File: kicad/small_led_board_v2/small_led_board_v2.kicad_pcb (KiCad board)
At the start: 2 copper layers, 83 parts, among them Q1 SQ2351CES, Q2 SQ2351CES, Q3 SQ2351CES, Q4 SQ2351CES, Q5 SQ2351CES, Q6 SQ2351CES, U1 74HCT541, U2 74HCT595, U3 TPIC6B595N

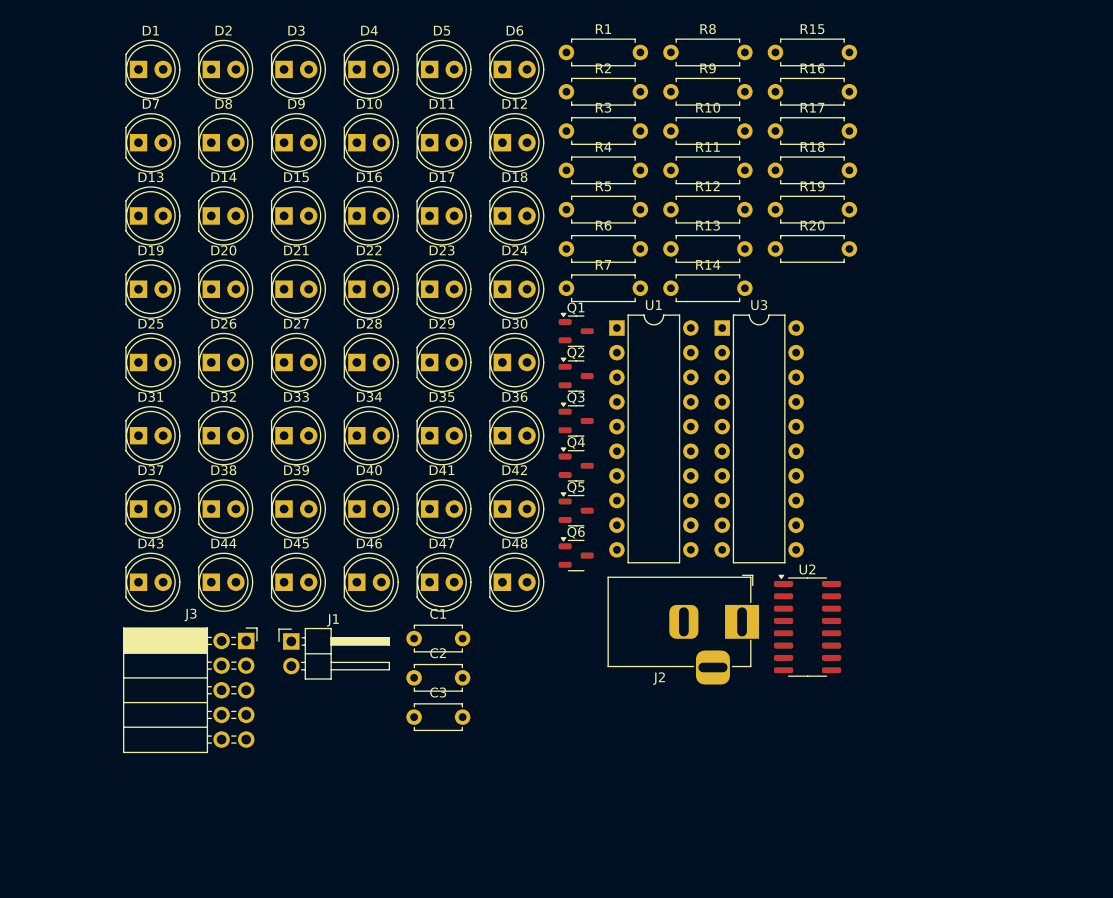
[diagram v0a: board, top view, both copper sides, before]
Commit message: small led board v2: placed components in general area
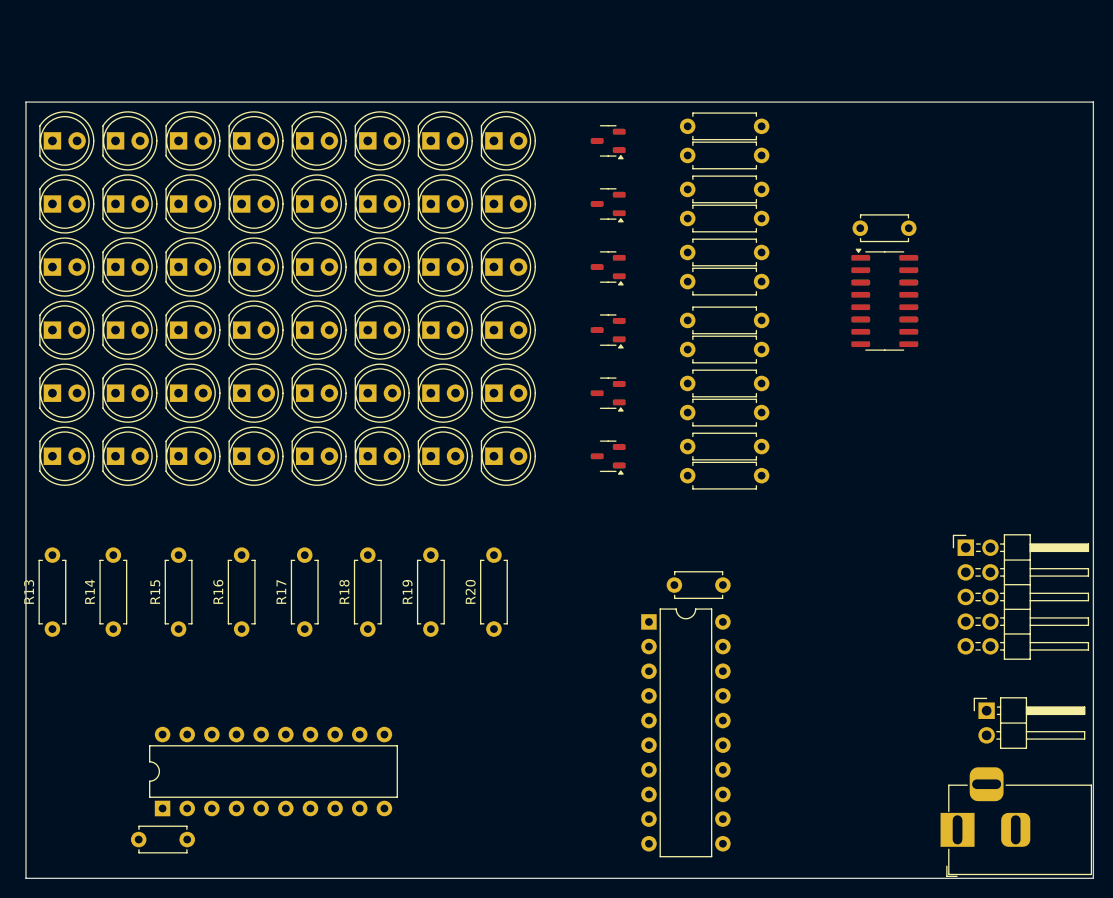
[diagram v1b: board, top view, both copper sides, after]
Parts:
- J3: footprint Connector_PinSocket_2.54mm:PinSocket_2x05_P2.54mm_Horizontal -> Connector_PinHeader_2.54mm:PinHeader_2x05_P2.54mm_Horizontal
- moved R15 85.5 mm to (65.7, 104.3), turned to 90 degrees
- moved R16 78.1 mm to (72.2, 104.3), turned to 90 degrees
- moved U3 76.0 mm to (64.1, 122.8), turned to 90 degrees
- moved R13 74.8 mm to (52.7, 104.3), turned to 90 degrees
- moved J3 74.8 mm to (146.8, 95.9)
- moved J1 72.0 mm to (149.0, 112.7)
- moved R17 70.6 mm to (78.7, 104.3), turned to 90 degrees
- moved C2 68.9 mm to (141.0, 63.0), turned to 180 degrees
- moved R14 67.3 mm to (59.0, 104.3), turned to 90 degrees
- moved R18 63.2 mm to (85.2, 104.3), turned to 90 degrees
- moved R19 55.9 mm to (91.7, 104.3), turned to 90 degrees
- moved R20 48.7 mm to (98.2, 104.3), turned to 90 degrees
- moved D42 40.2 mm to (59.2, 86.5)
- moved D18 40.2 mm to (59.2, 67.0)
- moved D41 39.2 mm to (52.7, 86.5)
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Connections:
- J3 pad 2: ShiftRowData -> RowStrobe
- J3 pad 3: ApplyRowAndStrobe -> ShiftRowData
- J3 pad 4: unconnected-(J3-Pin_4-Pad4) -> ShiftRowStrobe
- J3 pad 5: GND -> ApplyRowAndStrobe
- J3 pad 6: RowStrobe -> OutputEnable
- J3 pad 7: ShiftRowStrobe -> unconnected-(J3-Pin_7-Pad7)
- J3 pad 8: OutputEnable -> unconnected-(J3-Pin_8-Pad8)
- J3 pad 9: unconnected-(J3-Pin_9-Pad9) -> GND
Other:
- board outline added: 110 x 80 mm

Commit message: small led board v2: routing done and plotted
Also it was sent off to a manufacturer without major fixes. Just to see how it goes.
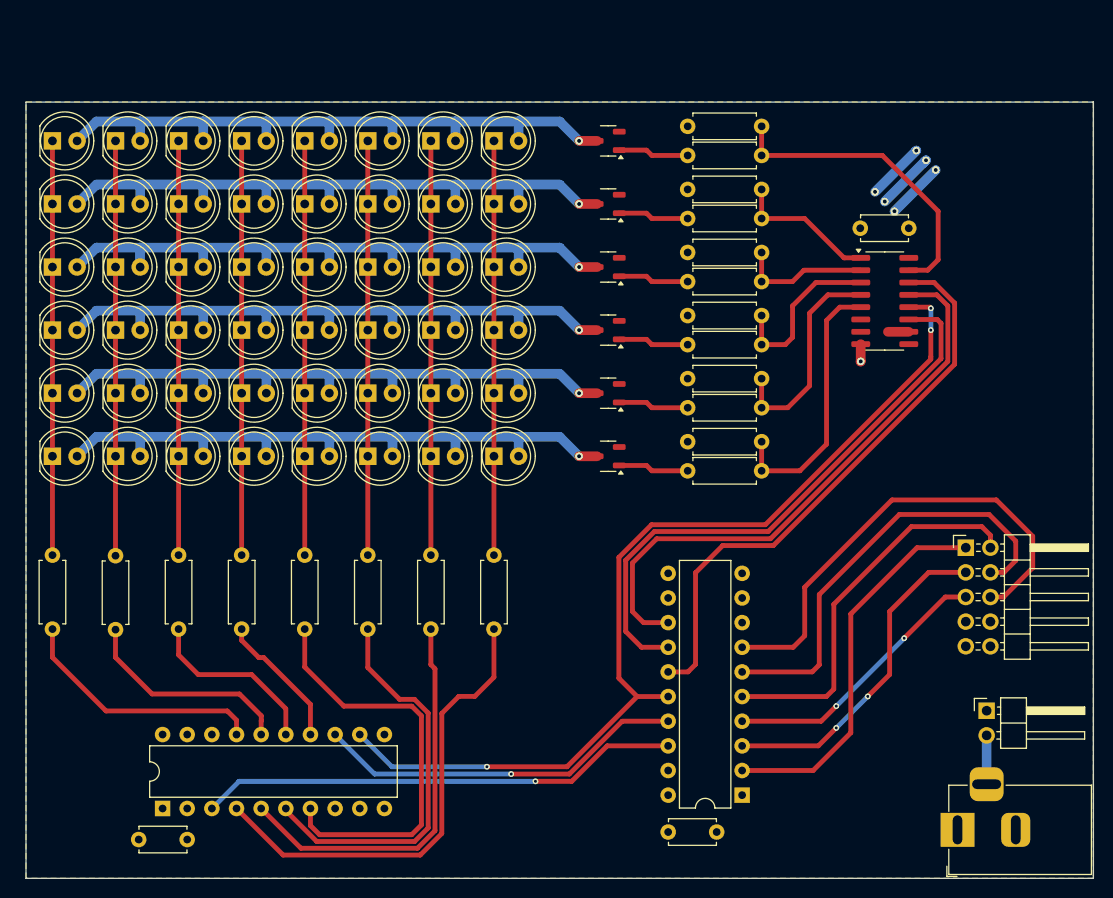
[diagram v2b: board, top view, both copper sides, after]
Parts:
- moved C1 26.1 mm to (116.2, 125.2), turned to 0 degrees
- moved U1 20.3 mm to (123.8, 121.4), turned to 180 degrees
- moved R10 0.50 mm to (118.2, 75.0)
- moved R11 0.50 mm to (118.2, 81.5)
- moved R12 0.50 mm to (118.2, 88.0)
- moved R4 0.50 mm to (118.2, 72.0)
- moved R5 0.50 mm to (118.2, 78.5)
- moved R6 0.50 mm to (118.2, 85.0)
- moved R14 0.23 mm to (59.2, 104.4)
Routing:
- net /ApplyRowAndStrobe': track 0.00 -> 99.5 mm, vias 0 -> 3
- net Net-(D25-A): track 0.00 -> 69.3 mm, vias 0 -> 1
- net Net-(D33-A): track 0.00 -> 69.3 mm, vias 0 -> 1
- net Net-(D17-A): track 0.00 -> 69.3 mm, vias 0 -> 1
- net Net-(D1-A): track 0.00 -> 69.3 mm, vias 0 -> 1
- net Net-(D41-A): track 0.00 -> 69.3 mm, vias 0 -> 1
- net Net-(D10-A): track 0.00 -> 69.3 mm, vias 0 -> 1
- net /ShiftRowStrobe': track 0.00 -> 60.6 mm
- net /OutputEnable': track 0.00 -> 60.5 mm
- net /RowStrobe': track 0.00 -> 60.1 mm
- net /RowData': track 0.00 -> 49.7 mm, vias 0 -> 1
- net OutputEnable: track 0.00 -> 49.6 mm
- net Net-(U3-DRAIN0): track 0.00 -> 48.3 mm
- net ShiftRowStrobe: track 0.00 -> 45.4 mm
- net Net-(U3-DRAIN3): track 0.00 -> 43.3 mm
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- added copper zone on F.Cu, net +5V
- added copper zone on B.Cu, net GND

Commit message: small led board v2: added missing pull ups to schematic and pcb
But the ordered PCB is obviously still missing those, they will be soldered on hacky on top just like it was meant to be.
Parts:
- added R21: R, Resistor_THT:R_Axial_DIN0207_L6.3mm_D2.5mm_P7.62mm_Horizontal, F.Cu at (108.4, 124.5)
- added R22: R, Resistor_THT:R_Axial_DIN0207_L6.3mm_D2.5mm_P7.62mm_Horizontal, F.Cu at (108.4, 127.5)
- added R23: R, Resistor_THT:R_Axial_DIN0207_L6.3mm_D2.5mm_P7.62mm_Horizontal, F.Cu at (126.1, 127.5)
- added R24: R, Resistor_THT:R_Axial_DIN0207_L6.3mm_D2.5mm_P7.62mm_Horizontal, F.Cu at (136.6, 127.5)
- added R25: R, Resistor_THT:R_Axial_DIN0207_L6.3mm_D2.5mm_P7.62mm_Horizontal, F.Cu at (136.6, 124.5)
- added R26: R, Resistor_THT:R_Axial_DIN0207_L6.3mm_D2.5mm_P7.62mm_Horizontal, F.Cu at (136.6, 121.5)
- moved C1 5.24 mm to (112.5, 121.5), turned to 180 degrees
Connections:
- net /OutputEnable' renamed /~{OutputEnable'}
- net OutputEnable renamed ~{OutputEnable}
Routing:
- net ~{OutputEnable}: track 49.6 -> 73.2 mm
- net ShiftRowStrobe: track 45.4 -> 68.9 mm
- net ApplyRowAndStrobe: track 28.4 -> 51.8 mm
- net RowStrobe: track 39.6 -> 60.1 mm
- net ShiftRowData: track 34.3 -> 52.2 mm
- net RowData: track 39.7 -> 54.6 mm

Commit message: small led board v2: updated resistor values
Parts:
- R13, R14, R15, R16, R17, R18, R19, R20: value R -> 56R
- R21, R22, R23, R24, R25, R26: value R -> 1M
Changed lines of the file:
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@@
 			)
 		)
-		(property "Value" "R"
+		(property "Value" "56R"
 			(at 3.81 2.37 90)
 			(layer "F.Fab")
@@
 			)
 		)
-		(property "Value" "R"
+		(property "Value" "56R"
 			(at 3.81 2.37 90)
 			(layer "F.Fab")
@@
 			)
 		)
-		(property "Value" "R"
+		(property "Value" "1M"
 			(at 3.81 2.37 0)
 			(layer "F.Fab")
@@
 			)
 		)
-		(property "Value" "R"
+		(property "Value" "56R"
 			(at 3.81 2.37 90)
 			(layer "F.Fab")
@@
 			)
 		)
-		(property "Value" "R"
+		(property "Value" "56R"
 			(at 3.81 2.37 90)
 			(layer "F.Fab")
@@
 			)
 		)
-		(property "Value" "R"
+		(property "Value" "56R"
 			(at 3.81 2.37 90)
 			(layer "F.Fab")
@@
 			)
 		)
-		(property "Value" "R"
+		(property "Value" "56R"
 			(at 3.81 2.37 90)
 			(layer "F.Fab")
@@
 			)
 		)
-		(property "Value" "R"
+		(property "Value" "1M"
 			(at 3.81 2.37 0)
 			(layer "F.Fab")
@@
 			)
 		)
-		(property "Value" "R"
+		(property "Value" "1M"
 			(at 3.81 2.37 0)
 			(layer "F.Fab")
@@
 			)
 		)
-		(property "Value" "R"
+		(property "Value" "56R"
 			(at 3.81 2.37 90)
 			(layer "F.Fab")
@@
 			)
 		)
-		(property "Value" "R"
+		(property "Value" "1M"
 			(at 3.81 2.37 0)
 			(layer "F.Fab")
@@
 			)
 		)
-		(property "Value" "R"
+		(property "Value" "1M"
 			(at 3.81 2.37 0)
 			(layer "F.Fab")
@@
 			)
 		)
-		(property "Value" "R"
+		(property "Value" "1M"
 			(at 3.81 2.37 0)
 			(layer "F.Fab")
@@
 			)
 		)
-		(property "Value" "R"
+		(property "Value" "56R"
 			(at 3.81 2.37 90)
 			(layer "F.Fab")

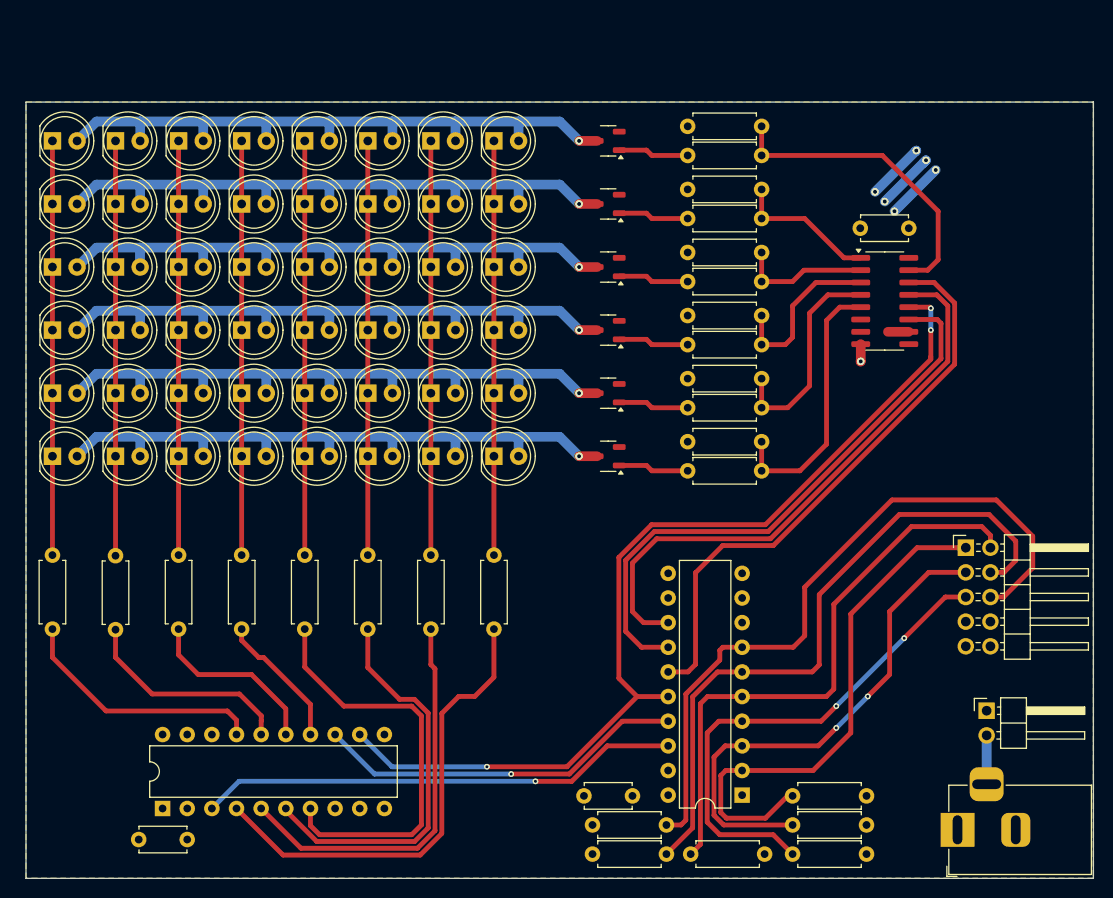
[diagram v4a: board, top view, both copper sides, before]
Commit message: kicad: migration complete to 9.0, small led boards both done
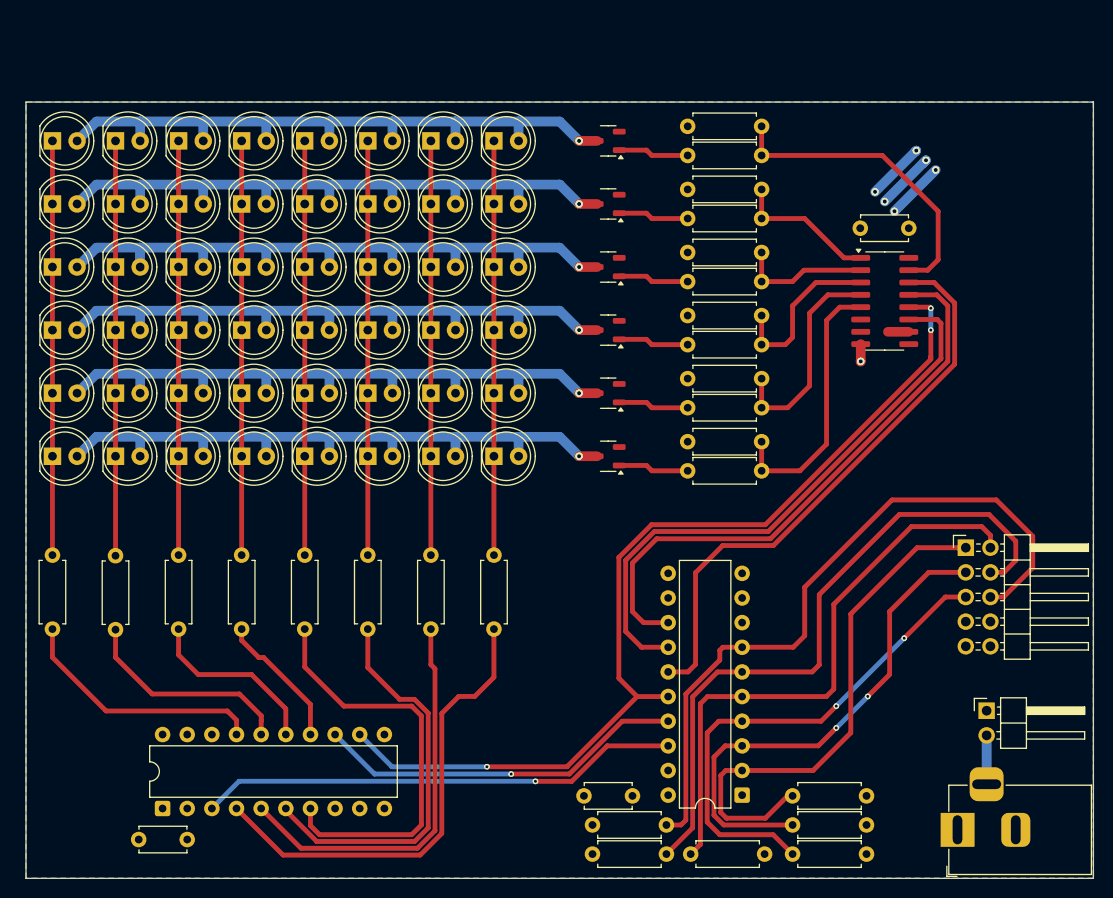
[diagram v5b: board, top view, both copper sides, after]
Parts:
- D1, D10, D11, D12, D13, D14, D15, D16, D17, D18, D19, D2, D20, D21, D22, D23, D24, D25, D26, D27, D28, D29, D3, D30, D31, D32, D33, D34, D35, D36, D37, D38, D39, D4, D40, D41, D42, D43, D44, D45, D46, D47, D48, D5, D6, D7, D8, D9: value ~ -> LED

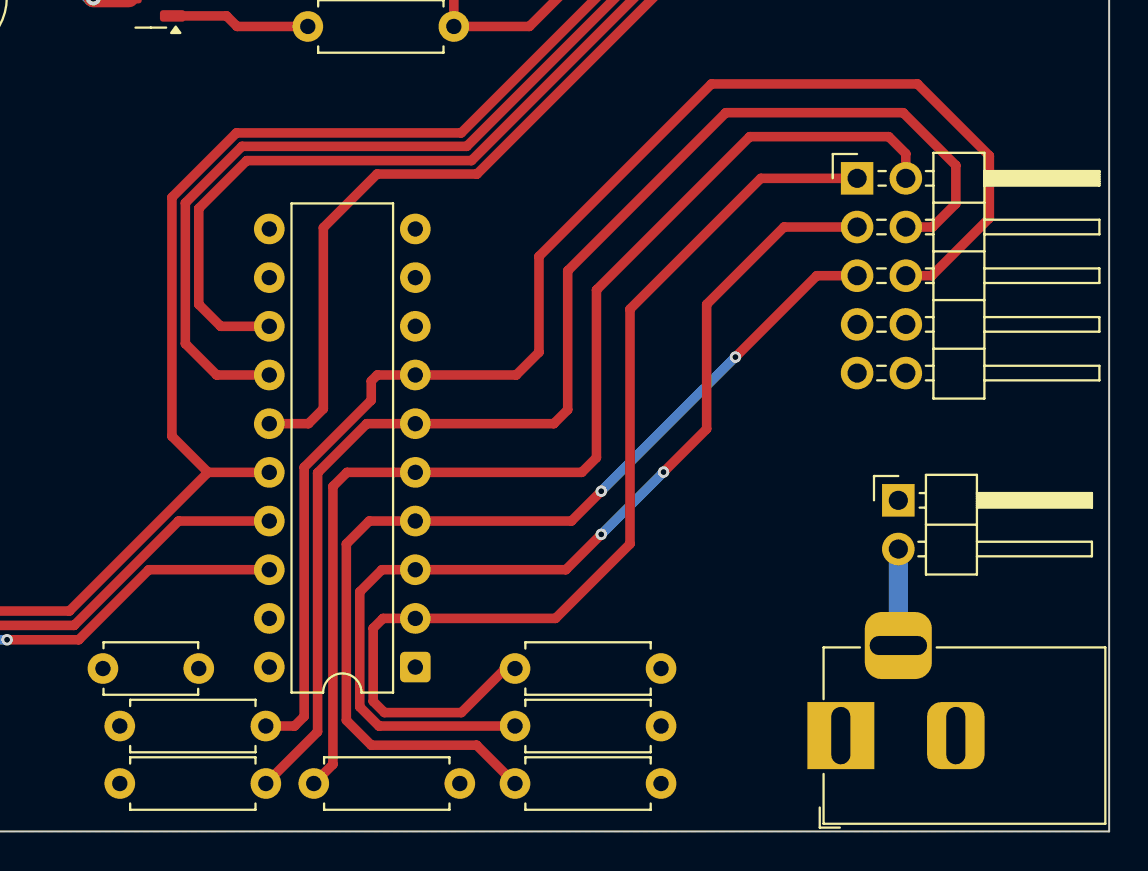
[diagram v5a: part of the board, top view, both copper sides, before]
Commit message: small led board v2: moved buffer pullups to +3.3v of pmod
This was a serious design oversight of not paying attention that the pullups could inject current into the FPGA IO when it's driven high (3.3V).
The only reason the FPGA survived this for so long is that the current was significantly limited by the pullups (10K/1M results in way too weak current) and an internal ESD diode possibly clamped the current.

The fullsize board is also affected and will be fixed in the next commit.
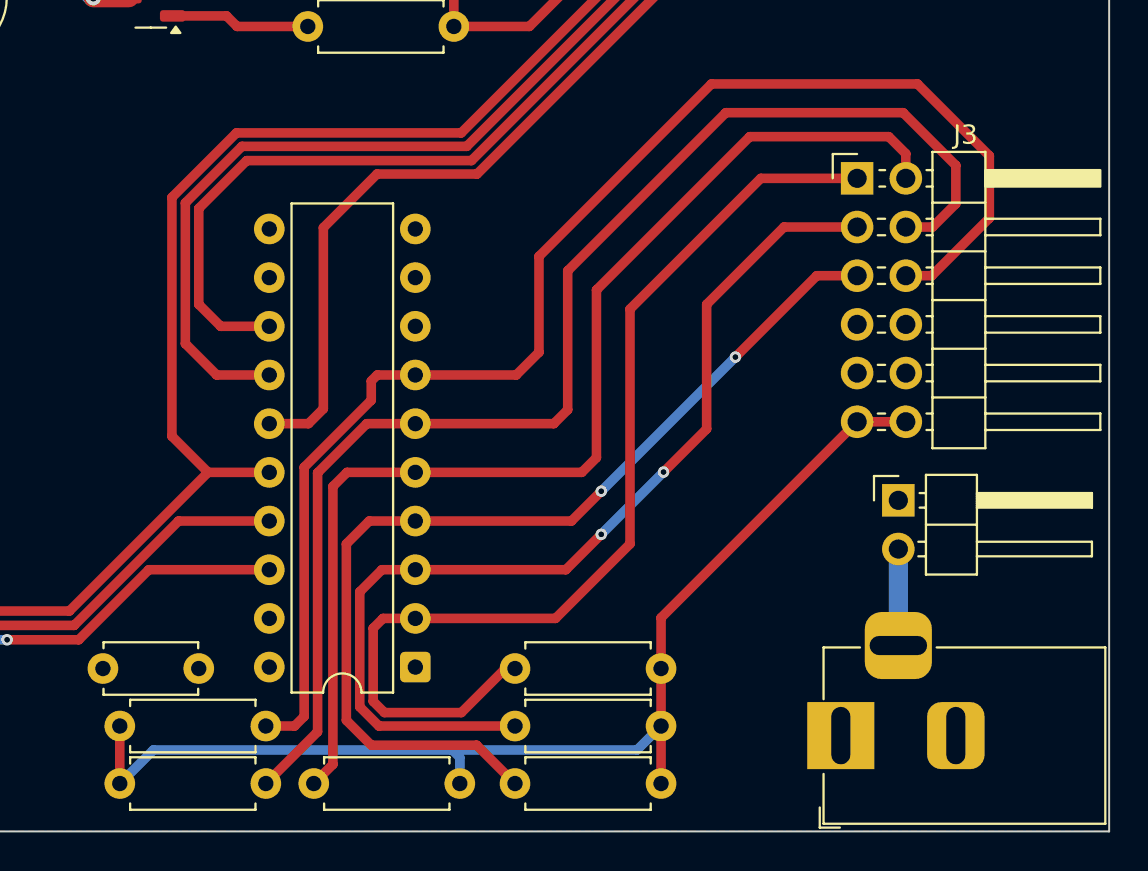
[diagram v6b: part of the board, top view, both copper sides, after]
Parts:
- J3: footprint Connector_PinHeader_2.54mm:PinHeader_2x05_P2.54mm_Horizontal -> Connector_PinHeader_2.54mm:PinHeader_2x06_P2.54mm_Horizontal
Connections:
- R21 pad 1: +5V -> 3.3V
- R22 pad 1: +5V -> 3.3V
- R23 pad 1: +5V -> 3.3V
- R24 pad 1: +5V -> 3.3V
- R25 pad 1: +5V -> 3.3V
- R26 pad 1: +5V -> 3.3V
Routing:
- net 3.3V: track 0.00 -> 60.0 mm
